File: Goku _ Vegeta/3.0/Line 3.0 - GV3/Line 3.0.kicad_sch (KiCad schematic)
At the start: 98 parts, among them J1 BATTERY POWER, J10 Motor 4, J11 LEFT HEADERS, J12 RIGHT HEADERS, J13 MID HEADERS, J2 BACKUP 5V, J3 BACKUP 3V3, J4 I2C, J6 Solenoid, J7 Motor 1, J8 Motor 2, J9 Motor 3, Q1 BSC040N10NS5, U3 LM2587S-ADJ, U4 TB67H420FTG Dual/Single Motor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, U5 TB67H420FTG Dual/Single Motor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, U6 TB67H420FTG Dual/Single Motor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, U7 TB67H420FTG Dual/Single Motor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, U8 DEV-16771

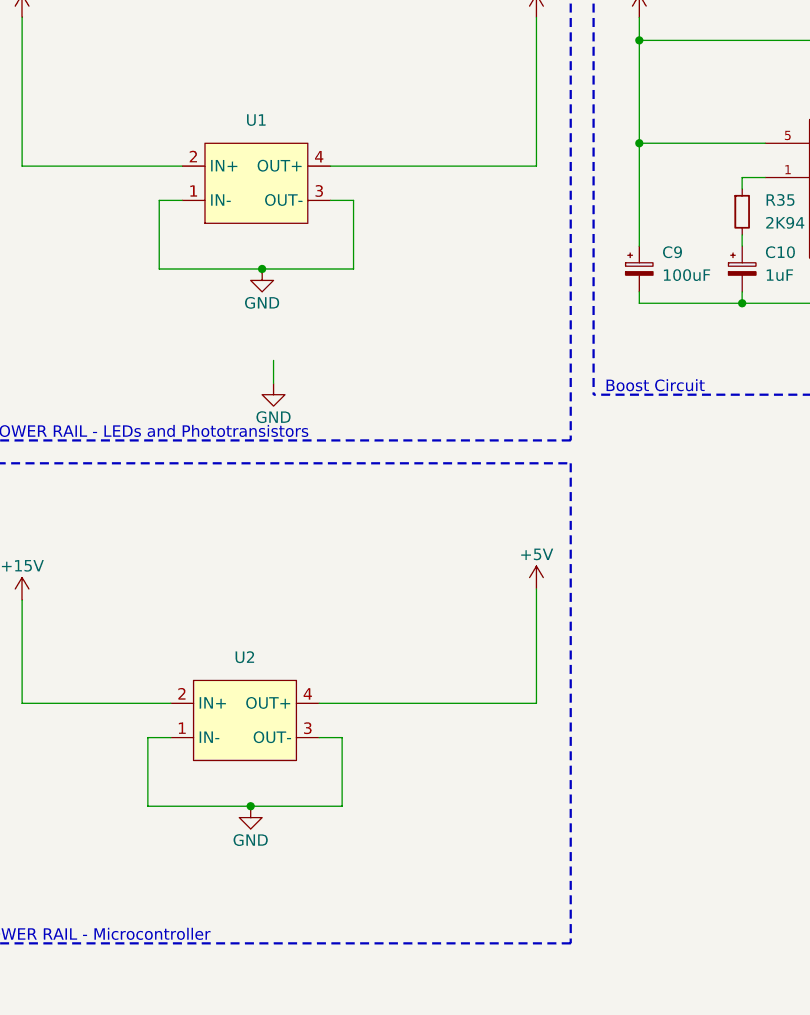
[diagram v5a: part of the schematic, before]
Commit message: LINE 3.0 Update
-Updated to have caps on power rails
-imrpoves tolerance of 100uf capacitor
-main power cable went from xt60 to xt30
- remove outer wheel guard
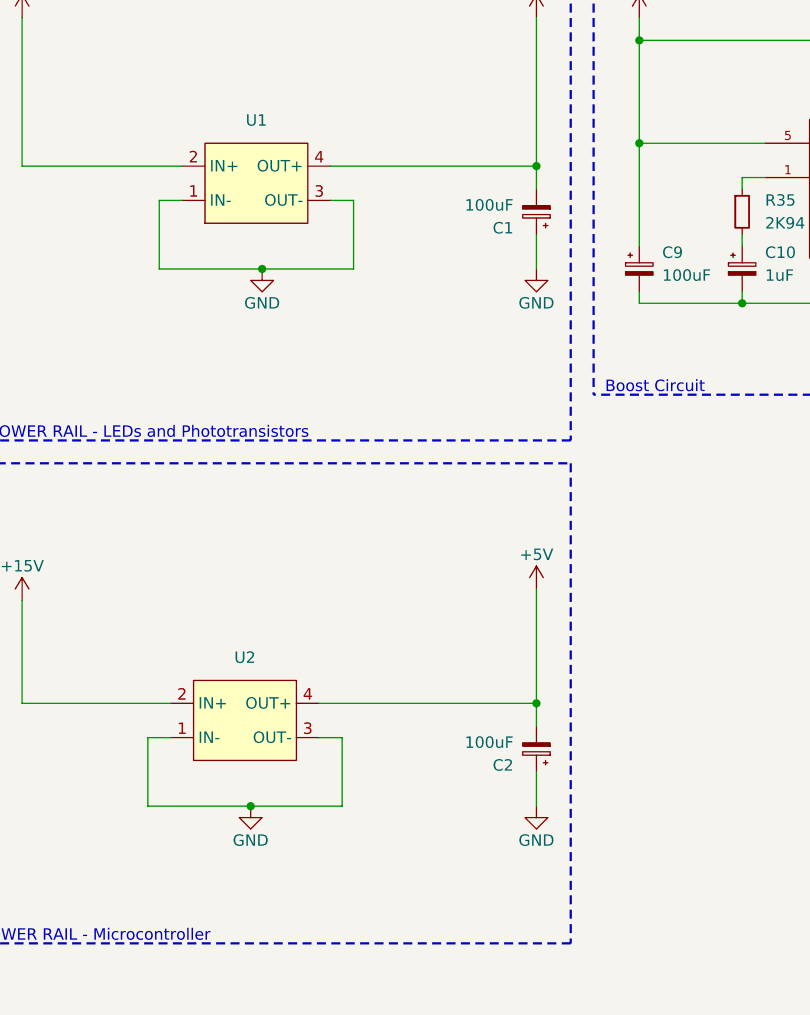
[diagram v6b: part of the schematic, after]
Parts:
- added C1, C2: 100uF, Capacitor_THT:CP_Radial_D10.0mm_P5.00mm, symbol Device:C_Polarized_Small
- J1: footprint Connector_AMASS:AMASS_XT60-F_1x02_P7.20mm_Vertical -> Connector_AMASS:AMASS_XT30U-F_1x02_P5.0mm_Vertical
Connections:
- net +3V3: now also C1.2
- net +5V: now also C2.2
- net GND: now also C1.1, C2.1
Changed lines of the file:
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@@
   (junction (at 318.77 27.94) (diameter 0) (color 0 0 0 0)
   )
+  (junction (at 205.74 101.6) (diameter 0) (color 0 0 0 0)
+  )
   (junction (at 74.93 243.84) (diameter 0) (color 0 0 0 0)
   )
@@
   (junction (at 27.94 25.4) (diameter 0) (color 0 0 0 0)
   )
+  (junction (at 205.74 41.91) (diameter 0) (color 0 0 0 0)
+  )
   (junction (at 27.94 213.36) (diameter 0) (color 0 0 0 0)
   )
@@
     (stroke (width 0) (type default))
   )
+  (wire (pts (xy 205.74 44.45) (xy 205.74 41.91))
+    (stroke (width 0) (type default))
+  )
   (wire (pts (xy 368.3 34.29) (xy 375.92 34.29))
     (stroke (width 0) (type default))
@@
     (stroke (width 0) (type default))
   )
+  (wire (pts (xy 205.74 49.53) (xy 205.74 53.34))
+    (stroke (width 0) (type default))
+  )
   (wire (pts (xy 78.74 99.06) (xy 78.74 96.52))
     (stroke (width 0) (type default))
@@
     (stroke (width 0) (type default))
   )
+  (wire (pts (xy 205.74 109.22) (xy 205.74 113.03))
+    (stroke (width 0) (type default))
+  )
   (wire (pts (xy 217.17 39.37) (xy 217.17 50.8))
     (stroke (width 0) (type default))
@@
     (stroke (width 0) (type default))
   )
+  (wire (pts (xy 205.74 104.14) (xy 205.74 101.6))
+    (stroke (width 0) (type default))
+  )
   (wire (pts (xy 71.12 251.46) (xy 71.12 252.73))
     (stroke (width 0) (type default))
@@
     (stroke (width 0) (type default))
   )
-  (wire (pts (xy 176.53 63.5) (xy 176.53 66.04))
-    (stroke (width 0) (type default))
-  )
   (wire (pts (xy 337.82 57.15) (xy 340.36 57.15))
     (stroke (width 0) (type default))
@@
     )
   )
+  (symbol (lib_id "power:GND") (at 205.74 53.34 0) (unit 1)
+    (in_bom yes) (on_board yes) (dnp no)
+    (property "Reference" "#PWR057" (at 205.74 59.69 0)
+      (effects (font (size 1.27 1.27)) hide)
+    )
+    (property "Value" "GND" (at 205.74 57.15 0)
+      (effects (font (size 1.27 1.27)))
+    )
+    (property "Footprint" "" (at 205.74 53.34 0)
+      (effects (font (size 1.27 1.27)) hide)
+    )
+    (property "Datasheet" "" (at 205.74 53.34 0)
+      (effects (font (size 1.27 1.27)) hide)
+    )
+    (pin "1")
+    (instances
+      (project "Line 3.0"
+        (path "/d5c7bd24-918a-4dd6-9ba7-d38579daba08"
+          (reference "#PWR057") (unit 1)
+        )
+      )
+    )
+  )
   (symbol (lib_name "GND_1") (lib_id "power:GND") (at 417.83 44.45 0) (mirror y) (unit 1)
     (in_bom yes) (on_board yes) (dnp no)
@@
       (effects (font (size 1.27 1.27)))
     )
-    (property "Footprint" "Connector_AMASS:AMASS_XT60-F_1x02_P7.20mm_Vertical" (at 118.11 30.48 0)
+    (property "Footprint" "Connector_AMASS:AMASS_XT30U-F_1x02_P5.0mm_Vertical" (at 118.11 30.48 0)
       (effects (font (size 1.27 1.27)) hide)
     )
@@
     )
   )
-  (symbol (lib_id "power:GND") (at 176.53 66.04 0) (unit 1)
-    (in_bom yes) (on_board yes) (dnp no)
-    (property "Reference" "#PWR057" (at 176.53 72.39 0)
-      (effects (font (size 1.27 1.27)) hide)
-    )
-    (property "Value" "GND" (at 176.53 69.85 0)
-      (effects (font (size 1.27 1.27)))
-    )
-    (property "Footprint" "" (at 176.53 66.04 0)
-      (effects (font (size 1.27 1.27)) hide)
-    )
-    (property "Datasheet" "" (at 176.53 66.04 0)
-      (effects (font (size 1.27 1.27)) hide)
-    )
-    (pin "1")
-    (instances
-      (project "Line 3.0"
-        (path "/d5c7bd24-918a-4dd6-9ba7-d38579daba08"
-          (reference "#PWR057") (unit 1)
-        )
-      )
-    )
-  )
   (symbol (lib_id "power:+15V") (at 148.59 25.4 0) (unit 1)
     (in_bom yes) (on_board yes) (dnp no)
@@
     )
   )
+  (symbol (lib_id "power:GND") (at 205.74 113.03 0) (unit 1)
+    (in_bom yes) (on_board yes) (dnp no)
+    (property "Reference" "#PWR094" (at 205.74 119.38 0)
+      (effects (font (size 1.27 1.27)) hide)
+    )
+    (property "Value" "GND" (at 205.74 116.84 0)
+      (effects (font (size 1.27 1.27)))
+    )
+    (property "Footprint" "" (at 205.74 113.03 0)
+      (effects (font (size 1.27 1.27)) hide)
+    )
+    (property "Datasheet" "" (at 205.74 113.03 0)
+      (effects (font (size 1.27 1.27)) hide)
+    )
+    (pin "1")
+    (instances
+      (project "Line 3.0"
+        (path "/d5c7bd24-918a-4dd6-9ba7-d38579daba08"
+          (reference "#PWR094") (unit 1)
+        )
+      )
+    )
+  )
   (symbol (lib_id "Device:R_Small_US") (at 78.74 133.35 0) (mirror x) (unit 1)
     (in_bom yes) (on_board yes) (dnp no)
@@
     )
   )
+  (symbol (lib_id "Device:C_Polarized_Small") (at 205.74 46.99 180) (unit 1)
+    (in_bom yes) (on_board yes) (dnp no)
+    (property "Reference" "C1" (at 203.2 48.8061 0)
+      (effects (font (size 1.27 1.27)) (justify left))
+    )
+    (property "Value" "100uF" (at 203.2 46.2661 0)
+      (effects (font (size 1.27 1.27)) (justify left))
+    )
+    (property "Footprint" "Capacitor_THT:CP_Radial_D10.0mm_P5.00mm" (at 205.74 46.99 0)
+      (effects (font (size 1.27 1.27)) hide)
+    )
+    (property "Datasheet" "~" (at 205.74 46.99 0)
+      (effects (font (size 1.27 1.27)) hide)
+    )
+    (pin "1")
+    (pin "2")
+    (instances
+      (project "Line 3.0"
+        (path "/d5c7bd24-918a-4dd6-9ba7-d38579daba08"
+          (reference "C1") (unit 1)
+        )
+      )
+    )
+  )
   (symbol (lib_id "ALS-PT19-315C_L177_TR8:ALS-PT19-315C{slash}L177{slash}TR8") (at 34.29 248.92 0) (mirror y) (unit 1)
     (in_bom yes) (on_board yes) (dnp no)
@@
         )
       )
+    )
+  )
+  (symbol (lib_id "Device:C_Polarized_Small") (at 205.74 106.68 180) (unit 1)
+    (in_bom yes) (on_board yes) (dnp no)
+    (property "Reference" "C2" (at 203.2 108.4961 0)
+      (effects (font (size 1.27 1.27)) (justify left))
+    )
+    (property "Value" "100uF" (at 203.2 105.9561 0)
+      (effects (font (size 1.27 1.27)) (justify left))
+    )
+    (property "Footprint" "Capacitor_THT:CP_Radial_D10.0mm_P5.00mm" (at 205.74 106.68 0)
+      (effects (font (size 1.27 1.27)) hide)
+    )
+    (property "Datasheet" "~" (at 205.74 106.68 0)
+      (effects (font (size 1.27 1.27)) hide)
+    )
+    (pin "1")
+    (pin "2")
+    (instances
+      (project "Line 3.0"
+        (path "/d5c7bd24-918a-4dd6-9ba7-d38579daba08"
+          (reference "C2") (unit 1)
+        )
+      )
